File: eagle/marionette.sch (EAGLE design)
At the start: 483 parts, among them J12 IDC_RECEPTACLE_20PIN-S9172-ND, J13 CONN_HEADER_JTAG, J2 SP3T Jumper Switch, J22 ZX62D-B-5P8, J3 IDC_RECEPTACLE_2X20-S9175-ND, J5 CON_COAX_PWR_PJ-047AH-NO_MILL, J8 IDC_RECEPTACLE_2X20-S9175-ND, J9 IDC_RECEPTACLE_2X20-S9175-ND, M5002 IRFR9024NTRPBF, Q2 NFET_DUAL_DMN63D8LDW, Q3 AO3419, SW1 SW-MOM-TACTILE-B3F-1000, SW2 SW-MOM-TACTILE-B3F-1000, U1 SWITCH_74HC4066D, U10 LMV344, U11 STM32F427-STM32F427, U13 CON_HIROSE_DM3D(MICROSD), U14 USB3320, U15 SWITCH_74HC4066D, U17 LM3671, U2 FR014H5JZ, U3 MIC5305_MIC5305-3.3YD5, U4 DAC124S085CIMM, U40 MIC5305_MIC5305-3.3YD5, U41 MIC5305-MIC5305-1.8YD5, U5 MAX3051ESAESA+, U5002 TPS40200, U6 OPAMP_DUAL_MC4558CDT, U7 LMV344, U8 LMV344, U9 LMV344, X1 ABSO7

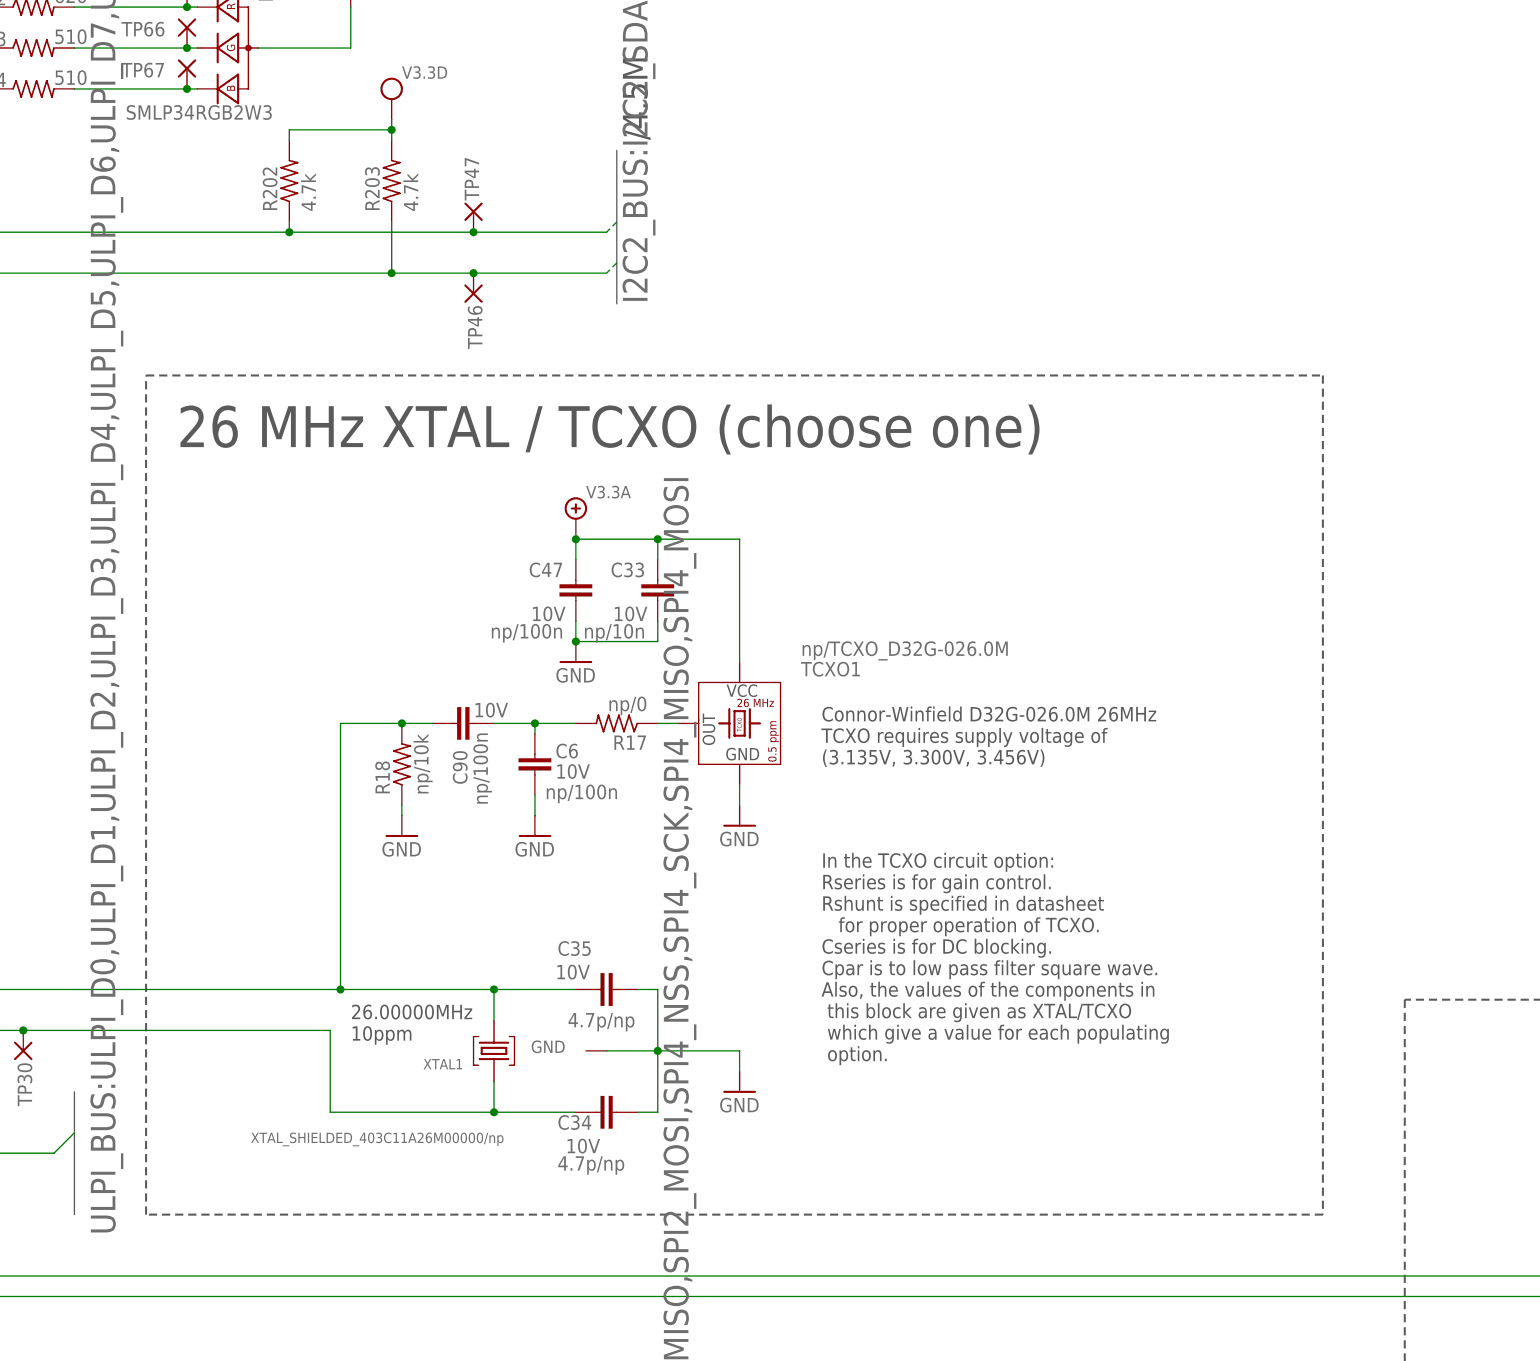
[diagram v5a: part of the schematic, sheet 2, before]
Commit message: Added IMPORTANT note regarding the clock input, namely, Silicon versions of STM32F427 before v3 will not enter bootloader properly if given an external clock signal, i.e. a TCXO.
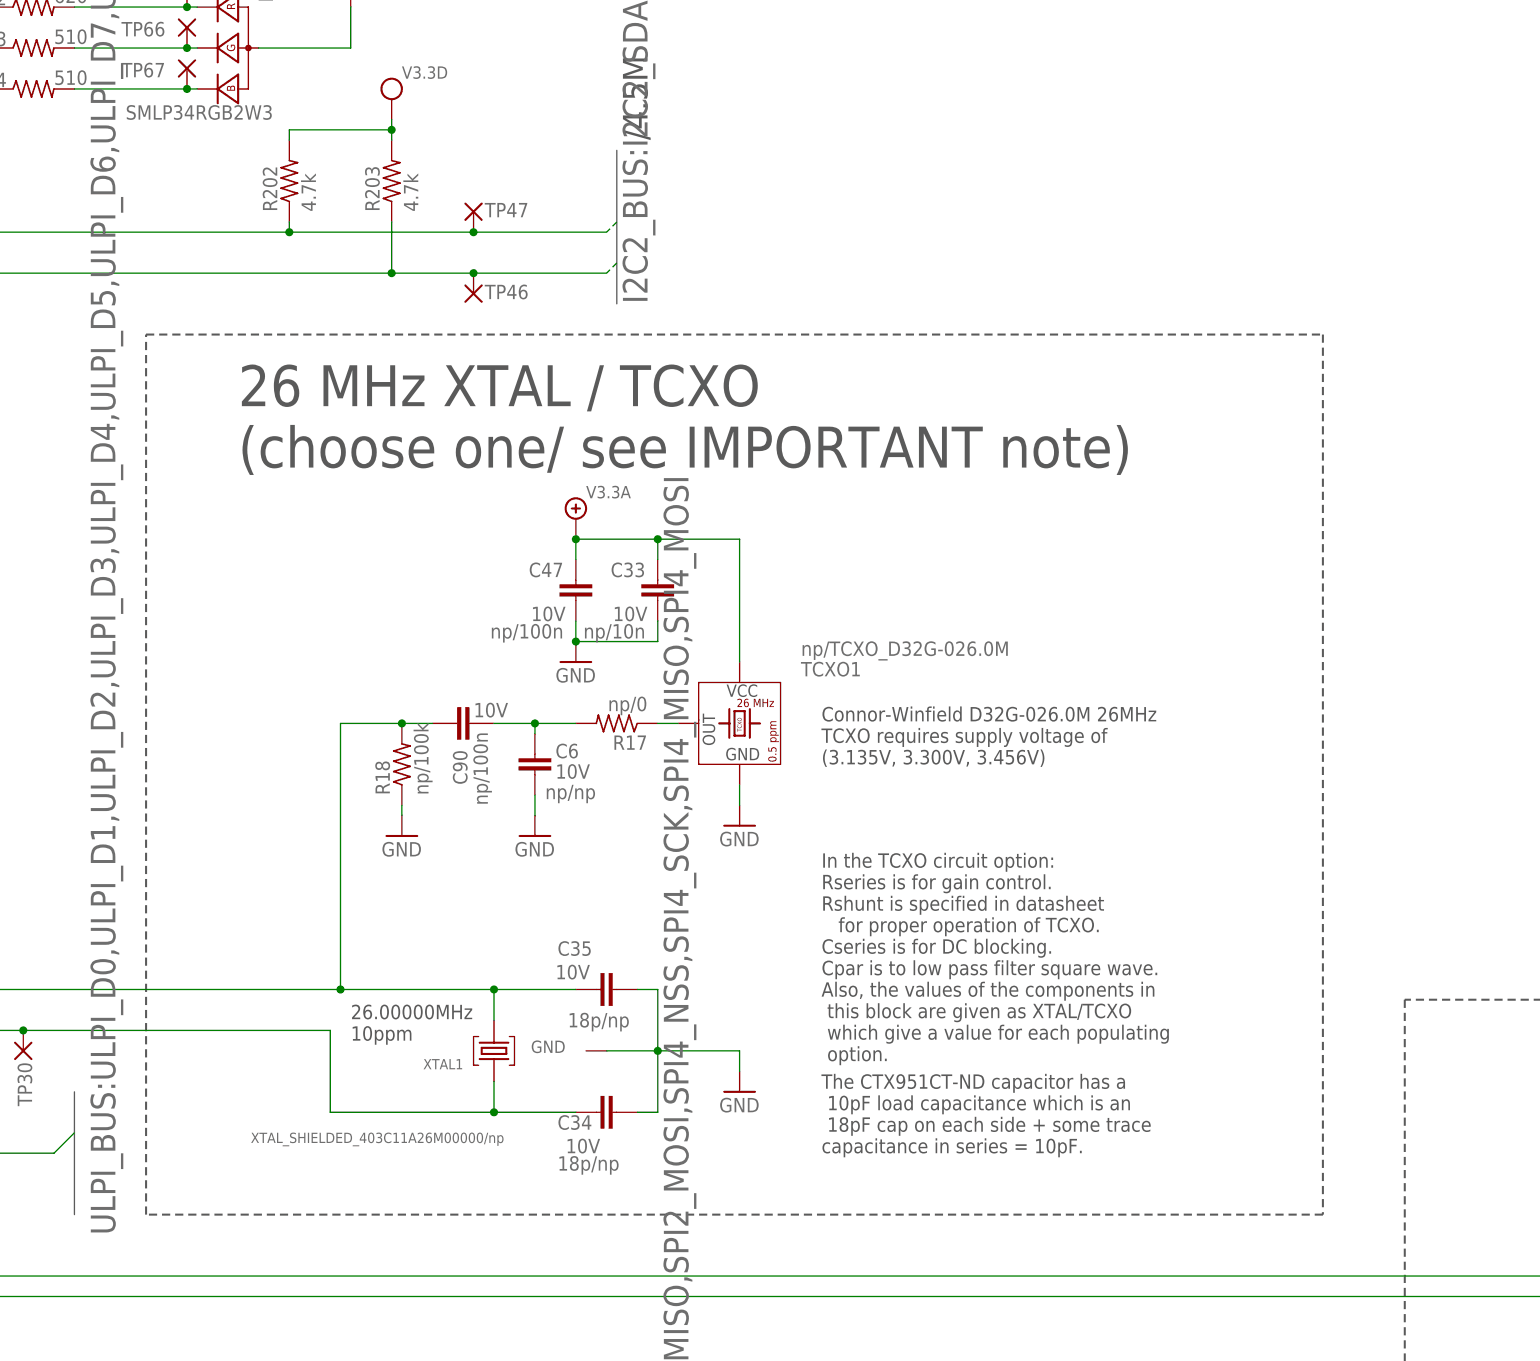
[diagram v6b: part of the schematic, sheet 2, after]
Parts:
- C34, C35: value 4.7p/np -> 18p/np
- C6: value np/100n -> np/np
- R18: value np/10k -> np/100k
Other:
- note added: "26 MHz XTAL / TCXO (choose one/ see IMPORTANT note)"
- note added: "IMPORTANT: versions of STM32F427 bootloader before version 9 (v9) will not boot if given an external clock signal (i.e. TCXO). Need chips made after 30th week of 2014 (datecode 430), with silicon revision 3. See STM32F40x Errata sheet v6 p35 (DM00037591.pdf) for an outline of how to read date codes and revisions. Basically you want a "3" to indicate version 3. Otherwise just use a standard crysta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"
- note added: "The CTX951CT-ND capacitor has a 10pF load capacitance which is an 18pF cap on each side + some trace capacitance in series = 10pF."
- note removed: "26 MHz XTAL / TCXO (choose one)"
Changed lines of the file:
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@@
 <part name="D3" library="marionette" deviceset="DIODE_SCHOTTKY-*" device="-BAS40-00_SOT23-3" value="BAS40-00"/>
 <part name="R19" library="rcl_custom" deviceset="R-US_" device="0402-B" value="1k"/>
-<part name="C34" library="rcl_custom" deviceset="C-EU" device="0402-B" value="4.7p/np">
+<part name="C34" library="rcl_custom" deviceset="C-EU" device="0402-B" value="18p/np">
 <attribute name="V_RATING" value="10V"/>
 </part>
-<part name="C35" library="rcl_custom" deviceset="C-EU" device="0402-B" value="4.7p/np">
+<part name="C35" library="rcl_custom" deviceset="C-EU" device="0402-B" value="18p/np">
 <attribute name="V_RATING" value="10V"/>
 </part>
@@
 <part name="V6" library="supply" deviceset="V3.3A" device=""/>
 <part name="R17" library="rcl_custom" deviceset="R-US_" device="0402-B" value="np/0"/>
-<part name="R18" library="rcl_custom" deviceset="R-US_" device="0402-B" value="np/10k"/>
+<part name="R18" library="rcl_custom" deviceset="R-US_" device="0402-B" value="np/100k"/>
 <part name="GND80" library="GROUND" deviceset="GND" device=""/>
 <part name="C90" library="rcl_custom" deviceset="C-EU" device="0402-B" value="np/100n">
@@
 <part name="R78" library="rcl_custom" deviceset="R-US_" device="0402-B" value="47k"/>
 <part name="TP30" library="marionette" deviceset="PAD+X" device="-0.7-NO_CREAM+SILK"/>
-<part name="C6" library="rcl_custom" deviceset="C-EU" device="0402-B" value="np/100n">
+<part name="C6" library="rcl_custom" deviceset="C-EU" device="0402-B" value="np/np">
 <attribute name="V_RATING" value="10V"/>
 </part>
@@
 <instance part="GND55" gate="G1" x="407.67" y="318.77"/>
 <instance part="V4" gate="G1" x="440.69" y="336.55"/>
-<instance part="U17" gate="G$1" x="341.63" y="326.39"/>
+<instance part="U17" gate="G1" x="341.63" y="326.39"/>
 <instance part="S4" gate="G1" x="520.7" y="327.66"/>
 <instance part="R75" gate="R" x="551.18" y="320.04" smashed="yes" rot="R270">
@@
 <pinref part="GND1" gate="G1" pin="GND"/>
 <wire x1="341.63" y1="308.61" x2="341.63" y2="311.15" width="0.1524" layer="91"/>
-<pinref part="U17" gate="G$1" pin="GND"/>
+<pinref part="U17" gate="G1" pin="GND"/>
 </segment>
 <segment>
@@
 <pinref part="R72" gate="R" pin="1"/>
 <wire x1="321.31" y1="334.01" x2="328.93" y2="334.01" width="0.1524" layer="91"/>
-<pinref part="U17" gate="G$1" pin="VIN"/>
+<pinref part="U17" gate="G1" pin="VIN"/>
 <pinref part="C2" gate="CE" pin="2"/>
 <wire x1="321.31" y1="334.01" x2="308.61" y2="334.01" width="0.1524" layer="91"/>
@@
 <wire x1="318.77" y1="323.85" x2="321.31" y2="323.85" width="0.1524" layer="91"/>
 <junction x="321.31" y="323.85"/>
-<pinref part="U17" gate="G$1" pin="EN"/>
+<pinref part="U17" gate="G1" pin="EN"/>
 <pinref part="TP200" gate="G1" pin="TP"/>
 <pinref part="TP1" gate="TP" pin="P"/>
@@
 <pinref part="L2" gate="G1" pin="2"/>
 <wire x1="354.33" y1="334.01" x2="359.41" y2="334.01" width="0.1524" layer="91"/>
-<pinref part="U17" gate="G$1" pin="SW"/>
+<pinref part="U17" gate="G1" pin="SW"/>
 </segment>
 </net>
@@
 <pinref part="C3" gate="CE" pin="2"/>
 <wire x1="382.27" y1="321.31" x2="382.27" y2="318.77" width="0.1524" layer="91"/>
-<pinref part="U17" gate="G$1" pin="FB"/>
+<pinref part="U17" gate="G1" pin="FB"/>
 <pinref part="TP82" gate="TP" pin="P"/>
 <junction x="369.57" y="321.31"/>
@@
  value of RS resistor controls
  output slope.</text>
-<wire x1="195.58" y1="337.82" x2="195.58" y2="441.96" width="0.254" layer="97" style="shortdash"/>
-<wire x1="195.58" y1="441.96" x2="341.63" y2="441.96" width="0.254" layer="97" style="shortdash"/>
-<wire x1="341.63" y1="441.96" x2="341.63" y2="337.82" width="0.254" layer="97" style="shortdash"/>
+<wire x1="195.58" y1="337.82" x2="195.58" y2="447.04" width="0.254" layer="97" style="shortdash"/>
+<wire x1="195.58" y1="447.04" x2="341.63" y2="447.04" width="0.254" layer="97" style="shortdash"/>
+<wire x1="341.63" y1="447.04" x2="341.63" y2="337.82" width="0.254" layer="97" style="shortdash"/>
 <wire x1="341.63" y1="337.82" x2="195.58" y2="337.82" width="0.254" layer="97" style="shortdash"/>
-<text x="199.39" y="433.07" size="5.08" layer="97">26 MHz XTAL / TCXO (choose one)</text>
+<text x="207.01" y="430.53" size="5.08" layer="97">26 MHz XTAL / TCXO
+(choose one/ see IMPORTANT note)</text>
 <wire x1="821.69" y1="699.77" x2="821.69" y2="631.19" width="0.254" layer="97" style="shortdash"/>
 <wire x1="821.69" y1="631.19" x2="951.23" y2="631.19" width="0.254" layer="97" style="shortdash"/>
@@
 demarcation of pin 1
 Digikey part no. in the device info.</text>
+<text x="279.4" y="345.44" size="1.778" layer="97">The CTX951CT-ND capacitor has a
+ 10pF load capacitance which is an
+ 18pF cap on each side + some trace
+capacitance in series = 10pF.</text>
+<text x="347.98" y="416.56" size="2.54" layer="112">IMPORTANT:
+versions of STM32F427 bootloader before version 9 (v9) will not boot if given an external clock signal
+(i.e. TCXO).  Need chips made after 30th week of 2014 (datecode 430), with silicon revision 3.  See
+ STM32F40x Errata sheet v6 p35 (DM00037591.pdf) for an outline of how to read date codes
+and revisions.  Basically you want a "3" to indicate version 3.  Otherwise just use a standard crystal
+ (which is driven by the STM OSC_OUT)</text>
 </plain>
 <instances>
@@
 <attribute name="VALUE" x="270.51" y="27.432" size="1.778" layer="96" rot="R180"/>
 </instance>
-<instance part="U5" gate="G$1" x="882.65" y="664.21"/>
+<instance part="U5" gate="G1" x="882.65" y="664.21"/>
 <instance part="GND28" gate="1" x="882.65" y="638.81"/>
 <instance part="C44" gate="CE" x="863.6" y="651.51" smashed="yes" rot="R180">
@@
 <instance part="V28" gate="G1" x="278.13" y="66.04"/>
 <instance part="V29" gate="G1" x="863.6" y="683.26"/>
-<instance part="TP46" gate="TP" x="236.22" y="452.12" rot="R270"/>
-<instance part="TP47" gate="TP" x="236.22" y="462.28" rot="R90"/>
+<instance part="TP46" gate="TP" x="236.22" y="452.12" smashed="yes" rot="R270">
+<attribute name="NAME" x="237.617" y="451.4342" size="1.778" layer="95"/>
+<attribute name="VALUE" x="232.918" y="453.263" size="1.778" layer="96" rot="R270"/>
+</instance>
+<instance part="TP47" gate="TP" x="236.22" y="462.28" smashed="yes" rot="R90">
+<attribute name="NAME" x="237.617" y="461.5942" size="1.778" layer="95"/>
+<attribute name="VALUE" x="239.522" y="461.137" size="1.778" layer="96" rot="R90"/>
+</instance>
 <instance part="TP72" gate="TP" x="853.44" y="659.13" rot="R270"/>
 <instance part="U1" gate="G1" x="504.19" y="280.67" smashed="yes" rot="MR180">
@@
 <segment>
 <pinref part="GND28" gate="1" pin="GND"/>
-<pinref part="U5" gate="G$1" pin="GND"/>
+<pinref part="U5" gate="G1" pin="GND"/>
 <wire x1="882.65" y1="641.35" x2="882.65" y2="643.89" width="0.1524" layer="91"/>
 <pinref part="C44" gate="CE" pin="1"/>
@@
 <net name="CAN1_TX" class="0">
 <segment>
-<pinref part="U5" gate="G$1" pin="TXD"/>
+<pinref part="U5" gate="G1" pin="TXD"/>
 <wire x1="864.87" y1="666.75" x2="850.9" y2="666.75" width="0.1524" layer="91"/>
 <label x="850.9" y="666.75" size="1.778" layer="95" rot="R180" xref="yes"/>
@@
 </segment>
 <segment>
-<pinref part="U5" gate="G$1" pin="RXD"/>
+<pinref part="U5" gate="G1" pin="RXD"/>
 <wire x1="836.93" y1="664.21" x2="864.87" y2="664.21" width="0.1524" layer="91"/>
 <label x="836.93" y="664.21" size="1.778" layer="95" rot="R180" xref="yes"/>
@@
 <wire x1="925.83" y1="671.83" x2="915.67" y2="671.83" width="0.1524" layer="91"/>
 <wire x1="915.67" y1="671.83" x2="915.67" y2="666.75" width="0.1524" layer="91"/>
-<pinref part="U5" gate="G$1" pin="CANH"/>
+<pinref part="U5" gate="G1" pin="CANH"/>
 <wire x1="915.67" y1="666.75" x2="900.43" y2="666.75" width="0.1524" layer="91"/>
 <pinref part="R29" gate="R" pin="2"/>
@@
 <wire x1="925.83" y1="659.13" x2="915.67" y2="659.13" width="0.1524" layer="91"/>
 <wire x1="915.67" y1="659.13" x2="915.67" y2="664.21" width="0.1524" layer="91"/>
-<pinref part="U5" gate="G$1" pin="CANL"/>
+<pinref part="U5" gate="G1" pin="CANL"/>
 <wire x1="915.67" y1="664.21" x2="900.43" y2="664.21" width="0.1524" layer="91"/>
 <pinref part="R29" gate="R" pin="1"/>
@@
 <segment>
 <wire x1="902.97" y1="659.13" x2="902.97" y2="656.59" width="0.1524" layer="91"/>
-<pinref part="U5" gate="G$1" pin="RS"/>
+<pinref part="U5" gate="G1" pin="RS"/>
 <wire x1="900.43" y1="659.13" x2="902.97" y2="659.13" width="0.1524" layer="91"/>
 <pinref part="R30" gate="R" pin="2"/>
@@
 <net name="CAN_SHDN" class="0">
 <segment>
-<pinref part="U5" gate="G$1" pin="SHDN"/>
+<pinref part="U5" gate="G1" pin="SHDN"/>
 <wire x1="864.87" y1="661.67" x2="858.52" y2="661.67" width="0.1524" layer="91"/>
 <label x="839.47" y="660.4" size="1.778" layer="95" rot="R180" xref="yes"/>
@@
 </segment>
 <segment>
-<pinref part="U5" gate="G$1" pin="VCC"/>
+<pinref part="U5" gate="G1" pin="VCC"/>
 <wire x1="863.6" y1="659.13" x2="864.87" y2="659.13" width="0.1524" layer="91"/>
 <pinref part="C44" gate="CE" pin="2"/>
